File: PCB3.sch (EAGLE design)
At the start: 138 parts

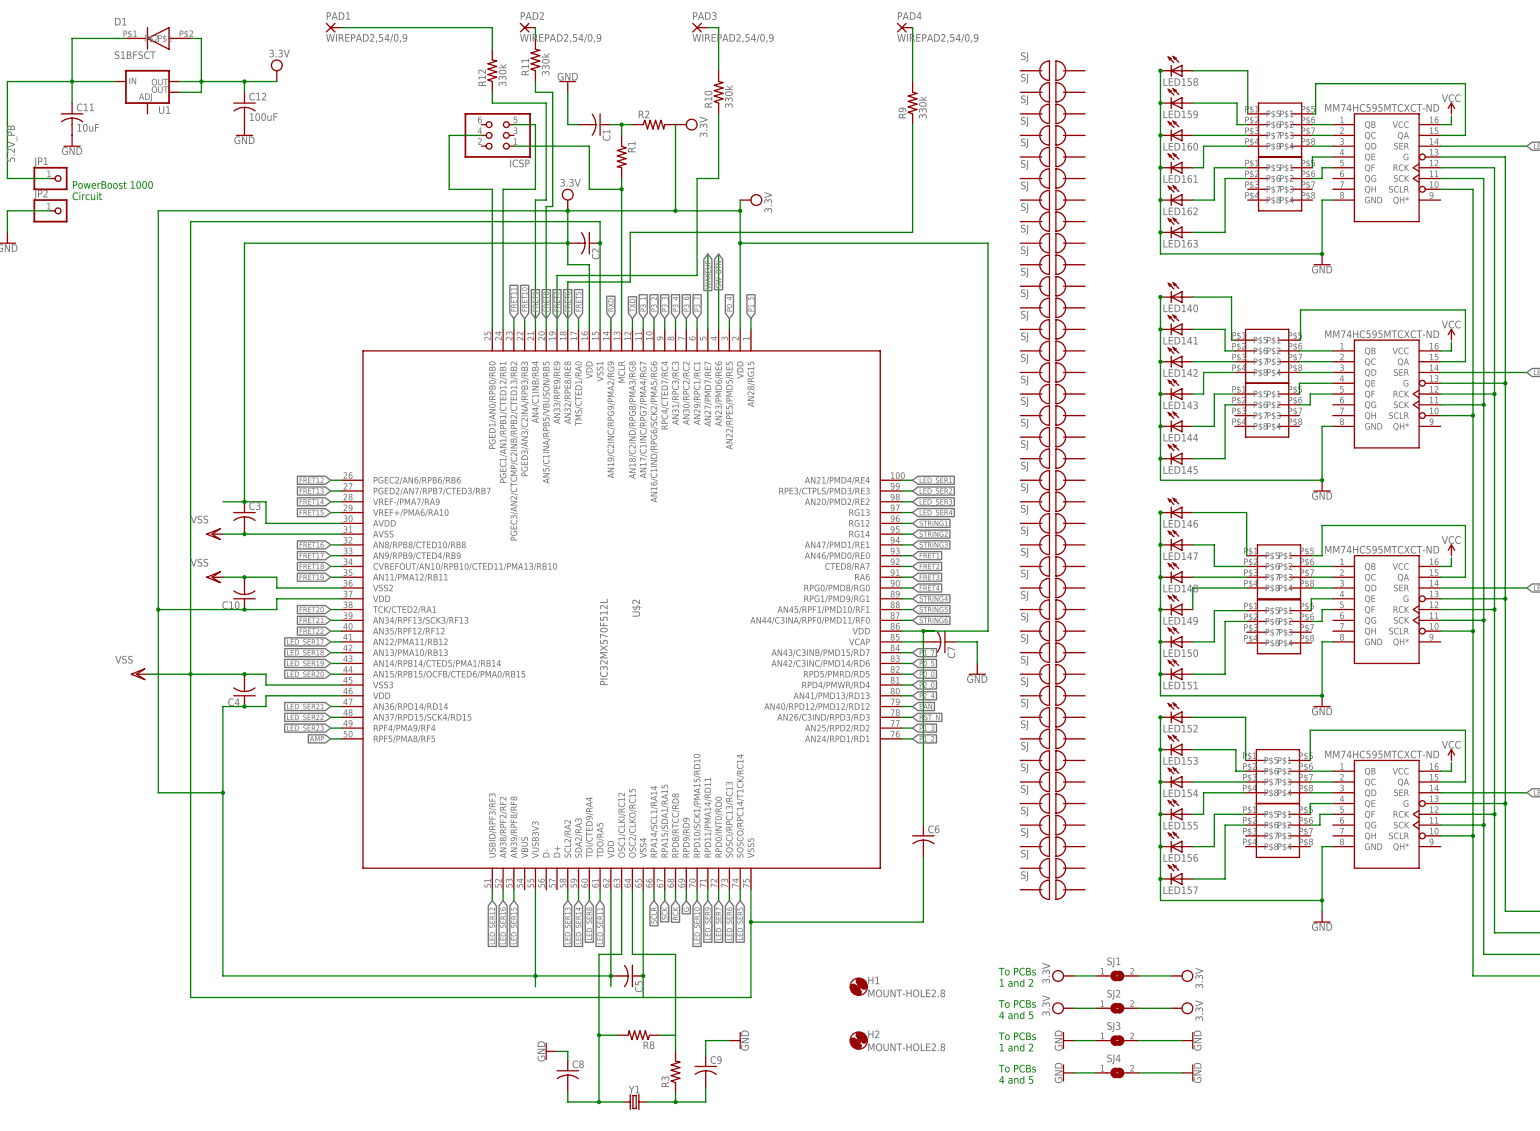
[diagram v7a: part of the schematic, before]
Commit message: Updated ref des to match those in BOM
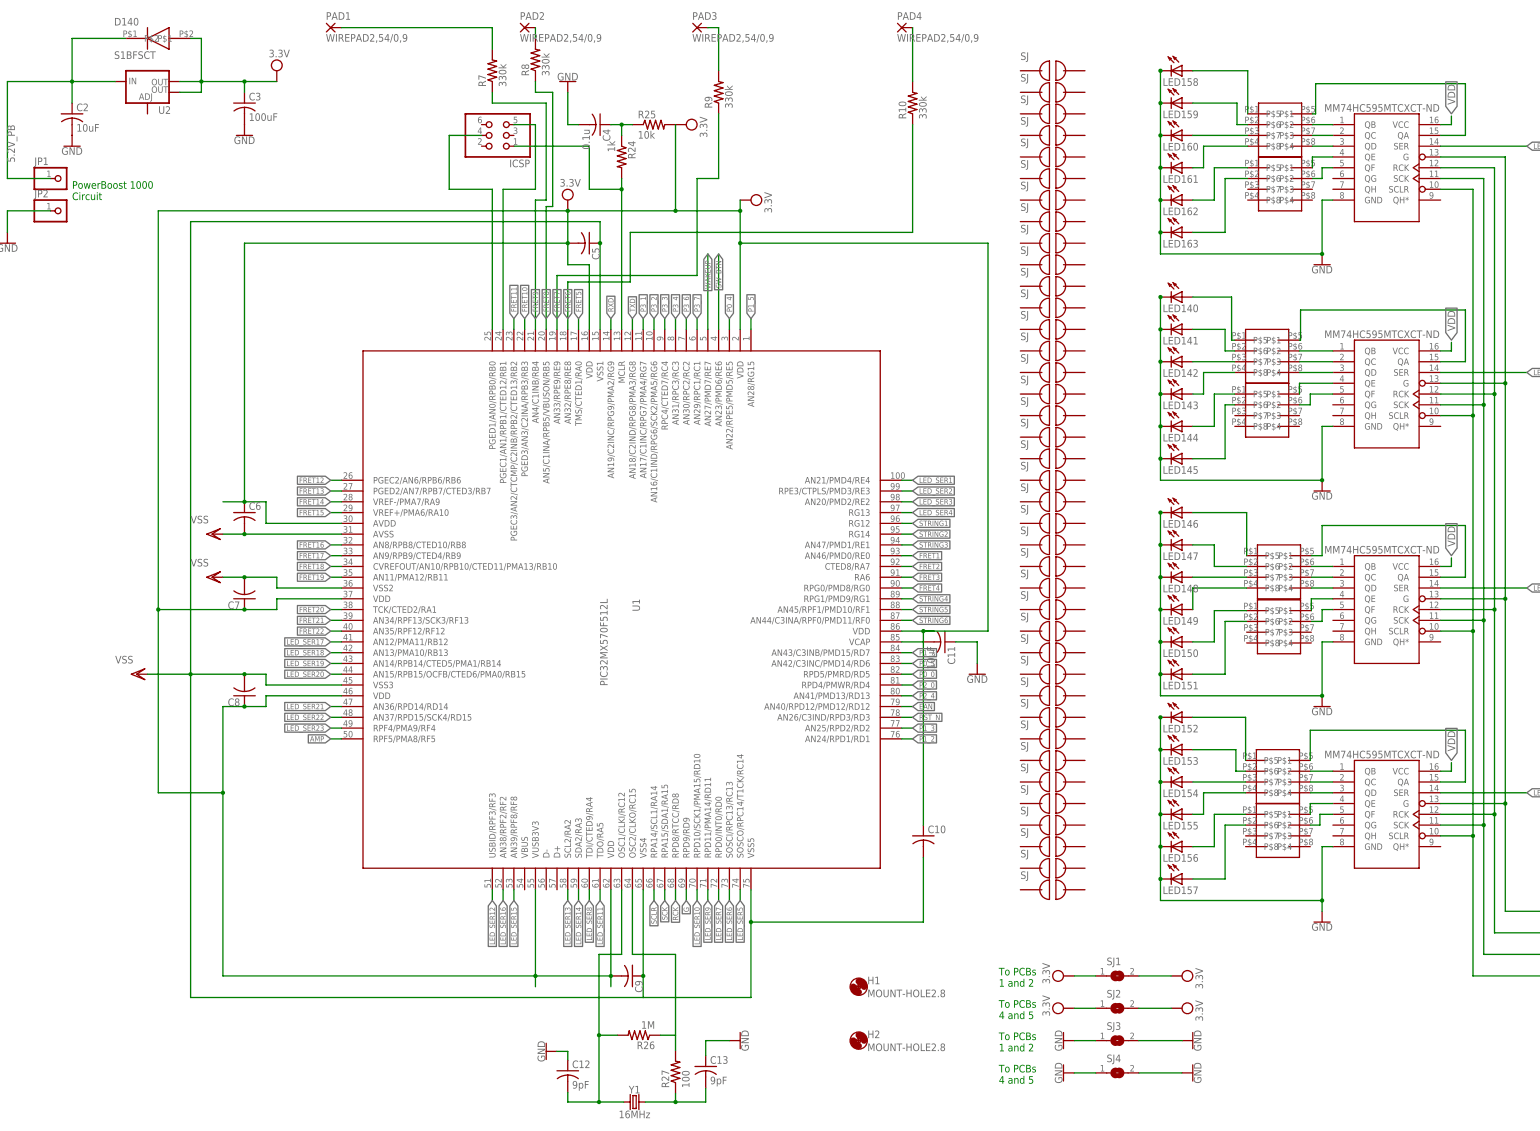
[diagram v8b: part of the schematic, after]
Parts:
- removed C1: (no value), rcl:C-USC0805
- removed R11: 330k, rcl:R-US_M0805
- removed U$2: PIC32MX570F512L, ECE477_Guitutar:PIC32MX570F512L
- added C13: 9pF, rcl:C-USC0805
- added R26: 1M, rcl:R-US_M0805
- added U2: (no value), SparkFun-IC-Power:V_REG_LM1117SOT223
- C12: value 100uF -> 9pF
- C2: value (none) -> 10uF
- C3: value (none) -> 100uF
- C4: value (none) -> 0.1u
- R24: value (none) -> 1k
- R25: value (none) -> 10k
- R27: value (none) -> 100
- R8: value (none) -> 330k
- U1: value (none) -> PIC32MX570F512L; device SparkFun-IC-Power:V_REG_LM1117SOT223 -> ECE477_Guitutar:PIC32MX570F512L
- Y1: value (none) -> 16MHz
- renumbered D1 to D140, R1 to R24, R12 to R7, R2 to R25, R3 to R27
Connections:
- removed net N$124: U$26.VCC
- removed net N$25: U$27.VCC
- removed net N$76: U$28.VCC
- removed net N$95: U$29.VCC
- net 5.2V_PB: now also C2.1, U2.IN; no longer C11.1, U1.IN
- net AMP: now also U1.RPF5/PMA8/RF5; no longer U$2.RPF5/PMA8/RF5
- net EAN: now also U1.AN40/RPD12/PMD12/RD12; no longer U$2.AN40/RPD12/PMD12/RD12
- net FRET1: now also U1.AN46/PMD0/RE0; no longer U$2.AN46/PMD0/RE0
- net FRET10: now also U1.PGED3/AN3/C2INA/RPB3/RB3; no longer U$2.PGED3/AN3/C2INA/RPB3/RB3
- net FRET11: now also U1.PGEC3/AN2/CTCMP/C2INB/RPB2/CTED13/RB2; no longer U$2.PGEC3/AN2/CTCMP/C2INB/RPB2/CTED13/RB2
- net FRET12: now also U1.PGEC2/AN6/RPB6/RB6; no longer U$2.PGEC2/AN6/RPB6/RB6
- net FRET13: now also U1.PGED2/AN7/RPB7/CTED3/RB7; no longer U$2.PGED2/AN7/RPB7/CTED3/RB7
- net FRET14: now also U1.VREF-/PMA7/RA9; no longer U$2.VREF-/PMA7/RA9
- net FRET15: now also U1.VREF+/PMA6/RA10; no longer U$2.VREF+/PMA6/RA10
- net FRET16: now also U1.AN8/RPB8/CTED10/RB8; no longer U$2.AN8/RPB8/CTED10/RB8
- net FRET17: now also U1.AN9/RPB9/CTED4/RB9; no longer U$2.AN9/RPB9/CTED4/RB9
- net FRET18: now also U1.CVREFOUT/AN10/RPB10/CTED11/PMA13/RB10; no longer U$2.CVREFOUT/AN10/RPB10/CTED11/PMA13/RB10
- net FRET19: now also U1.AN11/PMA12/RB11; no longer U$2.AN11/PMA12/RB11
- net FRET2: now also U1.CTED8/RA7; no longer U$2.CTED8/RA7
- net FRET20: now also U1.TCK/CTED2/RA1; no longer U$2.TCK/CTED2/RA1
- net FRET21: now also U1.AN34/RPF13/SCK3/RF13; no longer U$2.AN34/RPF13/SCK3/RF13
- net FRET22: now also U1.AN35/RPF12/RF12; no longer U$2.AN35/RPF12/RF12
- net FRET3: now also U1.RA6; no longer U$2.RA6
- net FRET4: now also U1.RPG0/PMD8/RG0; no longer U$2.RPG0/PMD8/RG0
- net FRET5: now also U1.TMS/CTED1/RA0; no longer U$2.TMS/CTED1/RA0
- net FRET6: now also R10.1, U1.AN32/RPE8/RE8; no longer R9.1, U$2.AN32/RPE8/RE8
- net FRET7: now also R9.1, U1.AN33/RPE9/RE9; no longer R10.1, U$2.AN33/RPE9/RE9
- net FRET8: now also R8.1, U1.AN5/C1INA/RPB5/VBUSON/RB5; no longer R11.1, U$2.AN5/C1INA/RPB5/VBUSON/RB5
- net FRET9: now also U1.AN4/C1INB/RB4; no longer U$2.AN4/C1INB/RB4
- net G: now also U1.RPD9/RD9; no longer U$2.RPD9/RD9
- net GND: now also C11.1, C12.1, C13.1, C2.2, C3.2, C4.2; no longer C1.2, C11.2, C12.2, C7.1, C8.1, C9.1
- net LED_SER1: now also U1.AN21/PMD4/RE4; no longer U$2.AN21/PMD4/RE4
- net LED_SER10: now also U1.RPD10/SCK1/PMA15/RD10; no longer U$2.RPD10/SCK1/PMA15/RD10
- net LED_SER11: now also U1.TDO/RA5; no longer U$2.TDO/RA5
- net LED_SER12: now also U1.USBID/RPF3/RF3; no longer U$2.USBID/RPF3/RF3
- net LED_SER13: now also U1.SCL2/RA2; no longer U$2.SCL2/RA2
- net LED_SER14: now also U1.SDA2/RA3; no longer U$2.SDA2/RA3
- net LED_SER15: now also U1.AN39/RPF8/RF8; no longer U$2.AN39/RPF8/RF8
- net LED_SER16: now also U1.AN38/RPF2/RF2; no longer U$2.AN38/RPF2/RF2
- net LED_SER17: now also U1.AN12/PMA11/RB12; no longer U$2.AN12/PMA11/RB12
- net LED_SER18: now also U1.AN13/PMA10/RB13; no longer U$2.AN13/PMA10/RB13
- net LED_SER19: now also U1.AN14/RPB14/CTED5/PMA1/RB14; no longer U$2.AN14/RPB14/CTED5/PMA1/RB14
- net LED_SER2: now also U1.RPE3/CTPLS/PMD3/RE3; no longer U$2.RPE3/CTPLS/PMD3/RE3
- net LED_SER20: now also U1.AN15/RPB15/OCFB/CTED6/PMA0/RB15; no longer U$2.AN15/RPB15/OCFB/CTED6/PMA0/RB15
- net LED_SER21: now also U1.AN36/RPD14/RD14; no longer U$2.AN36/RPD14/RD14
- net LED_SER22: now also U1.AN37/RPD15/SCK4/RD15; no longer U$2.AN37/RPD15/SCK4/RD15
- net LED_SER23: now also U1.RPF4/PMA9/RF4; no longer U$2.RPF4/PMA9/RF4
- net LED_SER3: now also U1.AN20/PMD2/RE2; no longer U$2.AN20/PMD2/RE2
- net LED_SER4: now also U1.RG13; no longer U$2.RG13
- net LED_SER5: now also U1.SOSCO/RPC14/T1CK/RC14; no longer U$2.SOSCO/RPC14/T1CK/RC14
- net LED_SER6: now also U1.SOSCI/RPC13/RC13; no longer U$2.SOSCI/RPC13/RC13
- net LED_SER7: now also U1.RPD0/INT0/RD0; no longer U$2.RPD0/INT0/RD0
- net LED_SER8: now also U1.TDI/CTED9/RA4; no longer U$2.TDI/CTED9/RA4
- net LED_SER9: now also U1.RPD11/PMA14/RD11; no longer U$2.RPD11/PMA14/RD11
- net N$1: now also C4.1; no longer C1.1
- net N$12: now also C11.2, U1.VCAP; no longer C7.2, U$2.VCAP
- net N$13: now also U1.MCLR; no longer U$2.MCLR
- net N$14: now also U1.PGED1/AN0/RPB0/RB0; no longer U$2.PGED1/AN0/RPB0/RB0
- net N$2: now also U1.PGEC1/AN1/RPB1/CTED12/RB1; no longer U$2.PGEC1/AN1/RPB1/CTED12/RB1
- net N$37: now also C13.2; no longer C9.2
- net N$38: now also C12.2, R26.2, U1.OSC1/CLKI/RC12; no longer C8.2, R8.2, U$2.OSC1/CLKI/RC12
- net N$4: now also R8.2; no longer R11.2
- net N$5: now also R9.2; no longer R10.2
- net N$7: now also R10.2; no longer R9.2
- net OSC2: now also R26.1, U1.OSC2/CLKO/RC15; no longer R8.1, U$2.OSC2/CLKO/RC15
- net P0_0: now also U1.RPD5/PMRD/RD5; no longer U$2.RPD5/PMRD/RD5
- net P0_4: now also U1.AN22/RPE5/PMD5/RE5; no longer U$2.AN22/RPE5/PMD5/RE5
- net P0_5: now also U1.AN42/C3INC/PMD14/RD6; no longer U$2.AN42/C3INC/PMD14/RD6
- net P1_2: now also U1.AN24/RPD1/RD1; no longer U$2.AN24/RPD1/RD1
- net P1_3: now also U1.AN25/RPD2/RD2; no longer U$2.AN25/RPD2/RD2
- net P1_5: now also U1.AN28/RG15; no longer U$2.AN28/RG15
- net P1_7: now also U1.AN43/C3INB/PMD15/RD7; no longer U$2.AN43/C3INB/PMD15/RD7
- net P2_0: now also U1.RPD4/PMWR/RD4; no longer U$2.RPD4/PMWR/RD4
- net P2_4: now also U1.AN41/PMD13/RD13; no longer U$2.AN41/PMD13/RD13
- net P3_1: now also U1.AN17/C1INC/RPG7/PMA4/RG7; no longer U$2.AN17/C1INC/RPG7/PMA4/RG7
- net P3_2: now also U1.AN16/C1IND/RPG6/SCK2/PMA5/RG6; no longer U$2.AN16/C1IND/RPG6/SCK2/PMA5/RG6
- net P3_3: now also U1.RPC4/CTED7/RC4; no longer U$2.RPC4/CTED7/RC4
- net P3_4: now also U1.AN31/RPC3/RC3; no longer U$2.AN31/RPC3/RC3
- net P3_6: now also U1.AN30/RPC2/RC2; no longer U$2.AN30/RPC2/RC2
- net P3_7: now also U1.AN29/RPC1/RC1; no longer U$2.AN29/RPC1/RC1
- net RCK: now also U1.RPD8/RTCC/RD8; no longer U$2.RPD8/RTCC/RD8
- net RST_N: now also U1.AN26/C3IND/RPD3/RD3; no longer U$2.AN26/C3IND/RPD3/RD3
- net RXD: now also U1.AN19/C2INC/RPG9/PMA2/RG9; no longer U$2.AN19/C2INC/RPG9/PMA2/RG9
- net SCK: now also U1.RPA15/SDA1/RA15; no longer U$2.RPA15/SDA1/RA15
- net SCLR: now also U1.RPA14/SCL1/RA14; no longer U$2.RPA14/SCL1/RA14
- net STRING1: now also U1.RG12; no longer U$2.RG12
- net STRING2: now also U1.RG14; no longer U$2.RG14
- net STRING3: now also U1.AN47/PMD1/RE1; no longer U$2.AN47/PMD1/RE1
- net STRING4: now also U1.RPG1/PMD9/RG1; no longer U$2.RPG1/PMD9/RG1
- net STRING5: now also U1.AN45/RPF1/PMD10/RF1; no longer U$2.AN45/RPF1/PMD10/RF1
- net STRING6: now also U1.AN44/C3INA/RPF0/PMD11/RF0; no longer U$2.AN44/C3INA/RPF0/PMD11/RF0
- net SW_BTN: now also U1.AN23/PMD6/RE6; no longer U$2.AN23/PMD6/RE6
- net TXD: now also U1.AN18/C2IND/RPG8/PMA3/RG8; no longer U$2.AN18/C2IND/RPG8/PMA3/RG8
- net VDD: now also C7.1, C8.1, C9.2, U$26.VCC, U$27.VCC, U$28.VCC, U$29.VCC, U1.AVDD, U1.VDD, U1.VDD@1, U1.VDD@2, U1.VDD@3, U1.VDD@4, U1.VDD@5, U1.VUSB3V3, U2.OUT, U2.OUT@1; no longer C12.1, C2.2, C4.1, U$2.AVDD, U$2.VDD, U$2.VDD@1, U$2.VDD@2, U$2.VDD@3, U$2.VDD@4, U$2.VDD@5, U$2.VUSB3V3, U1.OUT, U1.OUT@1
- net VSS: now also C7.2, C8.2, C9.1, U1.AVSS, U1.VSS1, U1.VSS2, U1.VSS3, U1.VSS4, U1.VSS5; no longer C2.1, C3.2, C4.2, U$2.AVSS, U$2.VSS1, U$2.VSS2, U$2.VSS3, U$2.VSS4, U$2.VSS5
- net WAKEUP: now also U1.AN27/PMD7/RE7; no longer U$2.AN27/PMD7/RE7
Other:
- moved on the sheet: C10, C11, C12, C2, C3, C4, C5, C6, C7, C8, C9, R10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
